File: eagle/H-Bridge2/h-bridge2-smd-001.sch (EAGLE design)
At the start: 28 parts

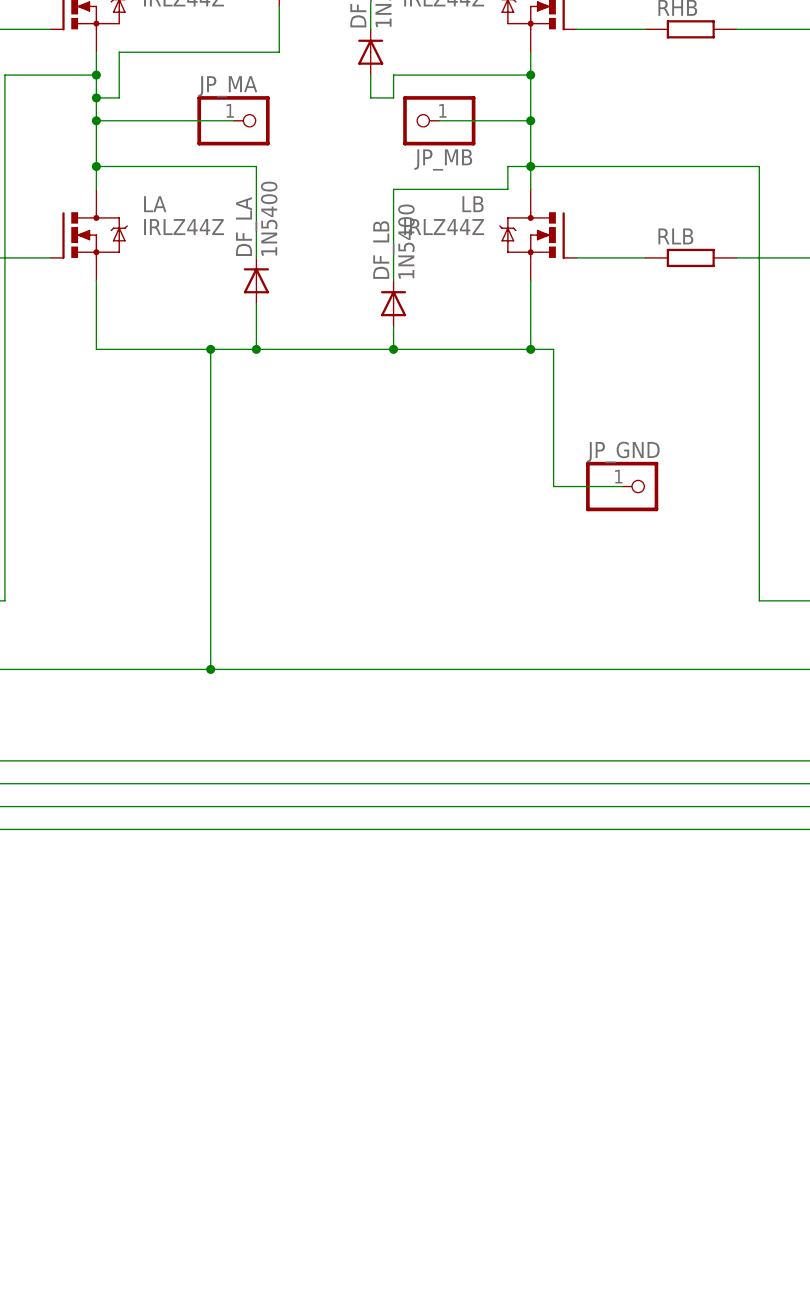
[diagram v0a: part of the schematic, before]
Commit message: SMD for logic drv
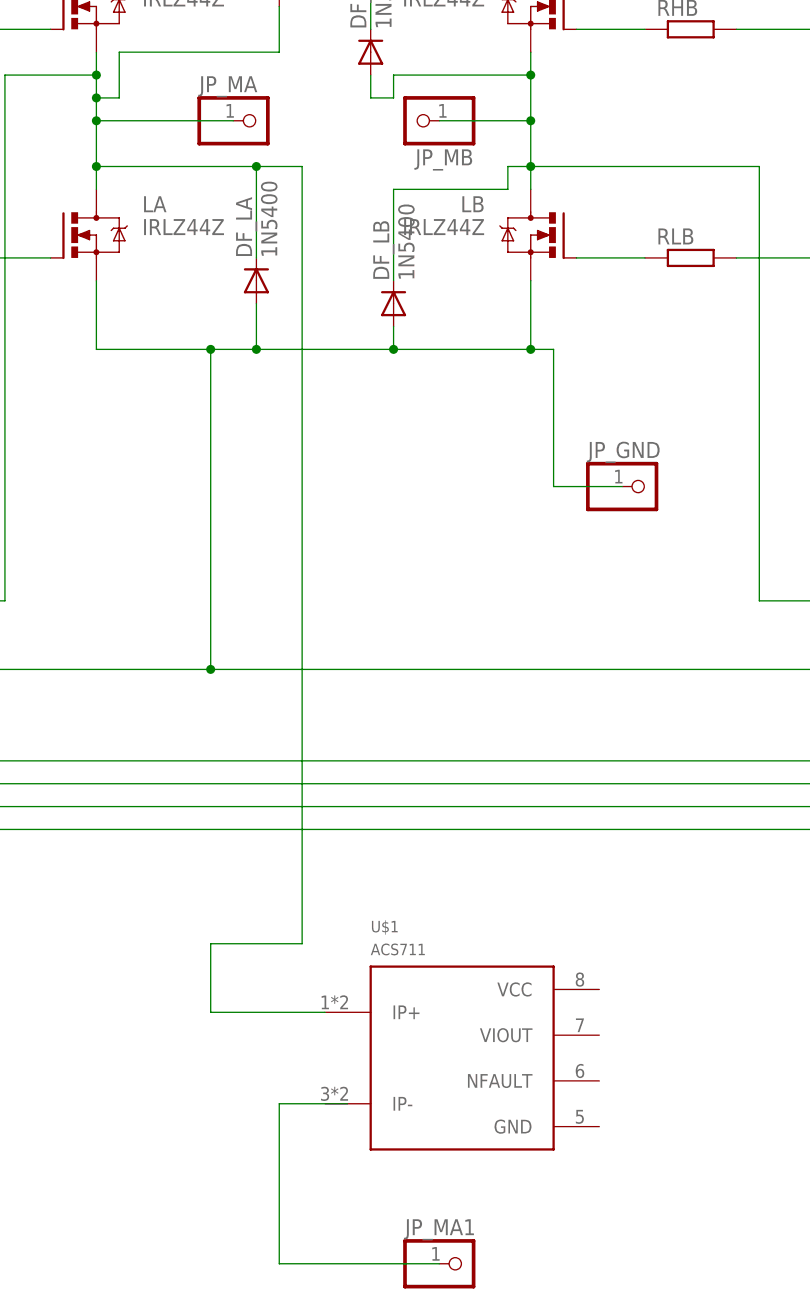
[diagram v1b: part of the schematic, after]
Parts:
- added JP_MA1: (no value), dbg-misc:PINHD-1X1
- added U$1: ACS711, acs711:ACS711
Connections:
- new net N$1: JP_MA1.1
- net N$17: now also U$1.IP+
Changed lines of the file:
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@@
 <part name="C3" library="rcl" deviceset="CPOL-EU" device="E5-13"/>
 <part name="C7" library="rcl" deviceset="CPOL-EU" device="E5-13"/>
+<part name="U$1" library="acs711" deviceset="ACS711" device=""/>
+<part name="JP_MA1" library="dbg-misc" deviceset="PINHD-1X1" device=""/>
 </parts>
 <sheets>
@@
 <instance part="C3" gate="G$1" x="5.08" y="25.4"/>
 <instance part="C7" gate="G$1" x="12.7" y="25.4"/>
+<instance part="U$1" gate="G$1" x="81.28" y="-48.26"/>
+<instance part="JP_MA1" gate="G$1" x="81.28" y="-71.12"/>
 </instances>
 <busses>
@@
 <wire x1="58.42" y1="50.8" x2="40.64" y2="50.8" width="0.1524" layer="91"/>
 <junction x="40.64" y="50.8"/>
+<pinref part="U$1" gate="G$1" pin="IP+"/>
+<wire x1="66.04" y1="-43.18" x2="53.34" y2="-43.18" width="0.1524" layer="91"/>
+<wire x1="53.34" y1="-43.18" x2="53.34" y2="-35.56" width="0.1524" layer="91"/>
+<wire x1="53.34" y1="-35.56" x2="63.5" y2="-35.56" width="0.1524" layer="91"/>
+<wire x1="63.5" y1="-35.56" x2="63.5" y2="50.8" width="0.1524" layer="91"/>
+<wire x1="63.5" y1="50.8" x2="58.42" y2="50.8" width="0.1524" layer="91"/>
+<junction x="58.42" y="50.8"/>
 </segment>
 </net>
@@
 </segment>
 </net>
+<net name="N$1" class="0">
+<segment>
+<wire x1="68.58" y1="-53.34" x2="60.96" y2="-53.34" width="0.1524" layer="91"/>
+<wire x1="60.96" y1="-53.34" x2="60.96" y2="-71.12" width="0.1524" layer="91"/>
+<pinref part="JP_MA1" gate="G$1" pin="1"/>
+<wire x1="60.96" y1="-71.12" x2="78.74" y2="-71.12" width="0.1524" layer="91"/>
+</segment>
+</net>
